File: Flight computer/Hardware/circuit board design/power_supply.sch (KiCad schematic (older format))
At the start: 11 parts, among them J2 USB_B_Micro, J4 Conn_01x02, U14 MAX40200AUK, U15 LD3985G33R_TSOT23, U9 STF202-22T1G

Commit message: updated the datasheet links and sites to purchase
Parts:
- J4: Cost (none) -> 0.38; Purchase link (none) -> https://uk.rs-online.com/web/p/pcb-headers/8201422/
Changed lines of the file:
@@
 F 1 "Conn_01x02" H 2568 3626 50  0000 C CNN
 F 2 "Connector_JST:JST_PH_B2B-PH-K_1x02_P2.00mm_Vertical" H 2650 3500 50  0001 C CNN
-F 3 "~" H 2650 3500 50  0001 C CNN
+F 3 "https://docs-emea.rs-online.com/webdocs/1347/0900766b81347511.pdf" H 2650 3500 50  0001 C CNN
+F 4 "0.38" H 2650 3500 50  0001 C CNN "Cost"
+F 5 "https://uk.rs-online.com/web/p/pcb-headers/8201422/" H 2650 3500 50  0001 C CNN "Purchase link"
 	1    2650 3500
 	-1   0    0    -1

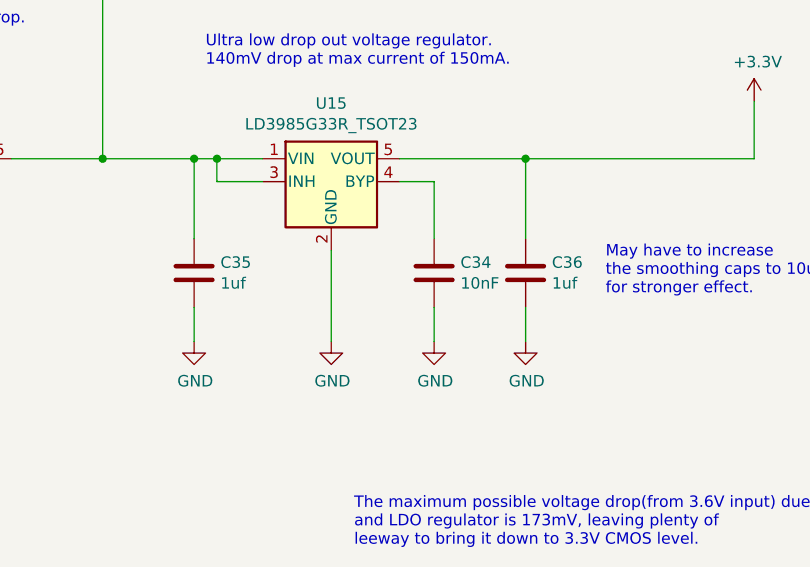
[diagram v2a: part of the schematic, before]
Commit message: added in the footprint for the 6 terminal block
routed the RF section with the 434 antenna
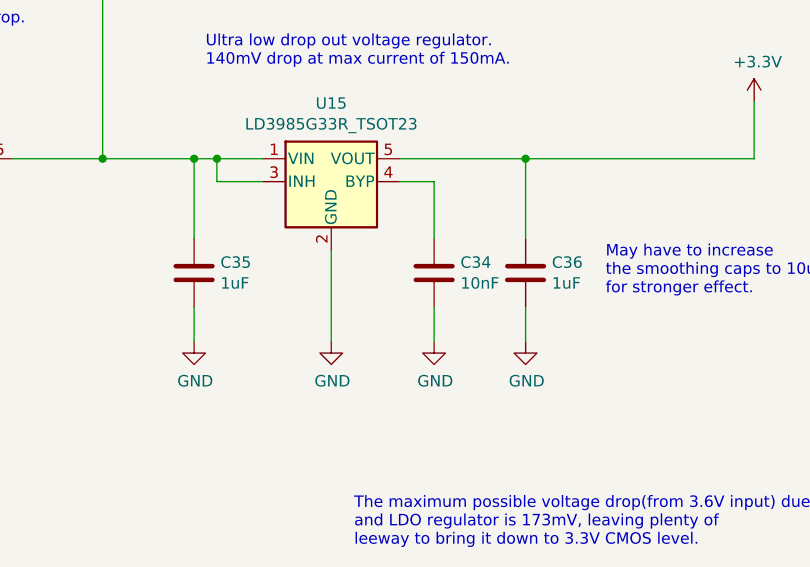
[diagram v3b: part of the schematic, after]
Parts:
- C34: footprint Capacitor_SMD:C_0603_1608Metric -> Capacitor_SMD:C_0402_1005Metric
- C35, C36: value 1uf -> 1uF
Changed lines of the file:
@@
 F 0 "C34" H 7815 4046 50  0000 L CNN
 F 1 "10nF" H 7815 3955 50  0000 L CNN
-F 2 "Capacitor_SMD:C_0603_1608Metric" H 7738 3850 50  0001 C CNN
+F 2 "Capacitor_SMD:C_0402_1005Metric" H 7738 3850 50  0001 C CNN
 F 3 "~" H 7700 4000 50  0001 C CNN
 	1    7700 4000
@@
 P 8100 4000
 F 0 "C36" H 8215 4046 50  0000 L CNN
-F 1 "1uf" H 8215 3955 50  0000 L CNN
+F 1 "1uF" H 8215 3955 50  0000 L CNN
 F 2 "Capacitor_SMD:C_0603_1608Metric" H 8138 3850 50  0001 C CNN
 F 3 "~" H 8100 4000 50  0001 C CNN
@@
 P 6650 4000
 F 0 "C35" H 6765 4046 50  0000 L CNN
-F 1 "1uf" H 6765 3955 50  0000 L CNN
+F 1 "1uF" H 6765 3955 50  0000 L CNN
 F 2 "Capacitor_SMD:C_0603_1608Metric" H 6688 3850 50  0001 C CNN
 F 3 "~" H 6650 4000 50  0001 C CNN

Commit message: added in molex usb 3D cad and silk screen ICSS logo
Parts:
- J2: footprint Connector_USB:USB_Micro-B_Molex-105017-0001 -> flight-computer:USB_Micro-B_Molex-105017-0001; Purchase link (none) -> https://www.mouser.co.uk/ProductDetail/Molex/105017-0001?qs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
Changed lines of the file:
@@
 F 0 "J2" H 1957 2267 50  0000 C CNN
 F 1 "USB_B_Micro" H 1957 2176 50  0000 C CNN
-F 2 "Connector_USB:USB_Micro-B_Molex-105017-0001" H 2050 1750 50  0001 C CNN
-F 3 "~" H 2050 1750 50  0001 C CNN
+F 2 "flight-computer:USB_Micro-B_Molex-105017-0001" H 2050 1750 50  0001 C CNN
+F 3 "https://www.molex.com/webdocs/datasheets/pdf/en-us/1050170001_IO_CONNECTORS.pdf" H 2050 1750 50  0001 C CNN
+F 4 "https://www.mouser.co.uk/ProductDetail/Molex/105017-0001?qs=sGAEpiMZZMulM8LPOQ%252BykxkHE97o%2FWJn1YkS%2FQp33f4%3D" H 1900 1800 50  0001 C CNN "Purchase link"
 	1    1900 1800
 	1    0    0    -1

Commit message: updated some of the purchase links
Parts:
- D3: Cost (none) -> 0.45; Purchase link (none) -> https://www.mouser.co.uk/ProductDetail/Diodes-Incorporated/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
- J2: Cost (none) -> 0.639
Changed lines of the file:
@@
 F 2 "Diode_SMD:D_PowerDI-123" H 5450 1700 50  0001 C CNN
 F 3 "https://www.diodes.com/assets/Datasheets/ds30492.pdf" H 5450 1700 50  0001 C CNN
+F 4 "0.45" H 5450 1700 50  0001 C CNN "Cost"
+F 5 "https://www.mouser.co.uk/ProductDetail/Diodes-Incorporated/DFLS130LQ-7?qs=sGAEpiMZZMtQ8nqTKtFS%2FIFUHrzpCXQh4E4plfym6vgtJOgQUsE5bw%3D%3D" H 5450 1700 50  0001 C CNN "Purchase link"
 	1    5450 1700
 	-1   0    0    1
@@
 F 3 "https://www.molex.com/webdocs/datasheets/pdf/en-us/1050170001_IO_CONNECTORS.pdf" H 2050 1750 50  0001 C CNN
 F 4 "https://www.mouser.co.uk/ProductDetail/Molex/105017-0001?qs=sGAEpiMZZMulM8LPOQ%252BykxkHE97o%2FWJn1YkS%2FQp33f4%3D" H 1900 1800 50  0001 C CNN "Purchase link"
+F 5 "0.639" H 1900 1800 50  0001 C CNN "Cost"
 	1    1900 1800
 	1    0    0    -1
